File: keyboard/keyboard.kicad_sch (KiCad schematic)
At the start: 64 parts, among them J1 Conn_01x04, J2 Conn_01x04, SW1 SW_Push, SW10 SW_Push, SW11 SW_Push, SW12 SW_Push, SW13 SW_Push, SW14 SW_Push, SW15 SW_Push, SW16 SW_Push, SW17 SW_Push, SW18 SW_Push, SW19 SW_Push, SW2 SW_Push, SW20 SW_Push, SW21 SW_Push, SW3 SW_Push, SW4 SW_Push, SW5 SW_Push, SW6 SW_Push, SW7 SW_Push, SW8 SW_Push, SW9 SW_Push, U1 AP2127K-3.3, U2 USBLC6-2SC6, U3 STM32F072CBTx

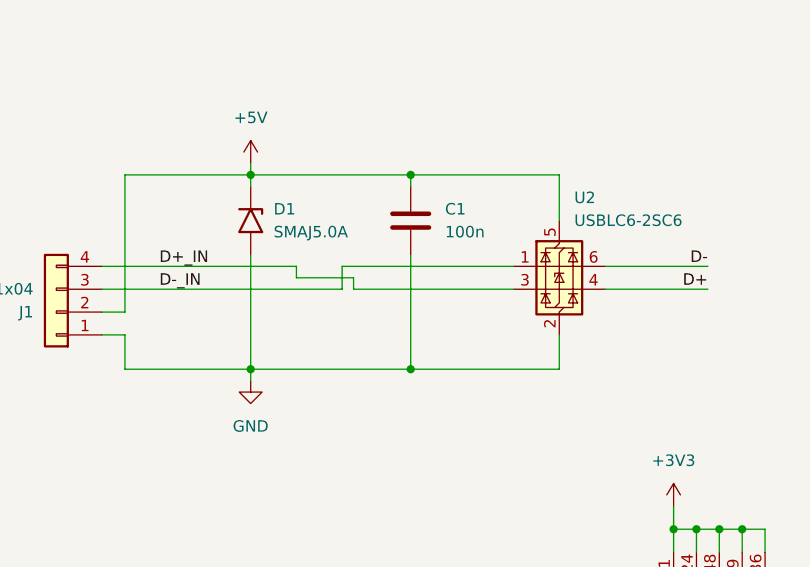
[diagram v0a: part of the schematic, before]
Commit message: Added board outlines 12mm from key switch centres.
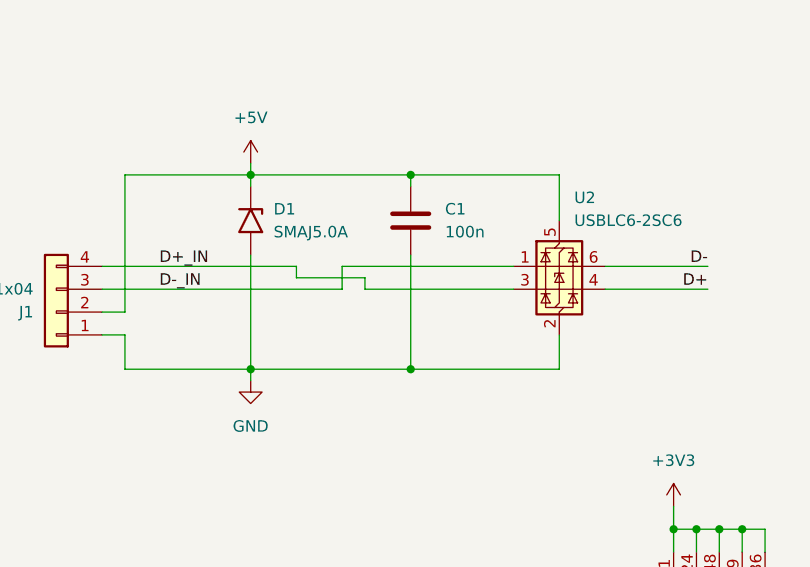
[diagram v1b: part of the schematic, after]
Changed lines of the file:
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@@
 	(wire
 		(pts
-			(xy 63.5 35.56) (xy 63.5 36.83)
+			(xy 64.77 35.56) (xy 64.77 36.83)
 		)
 		(stroke
@@
 	(wire
 		(pts
-			(xy 63.5 36.83) (xy 81.28 36.83)
+			(xy 64.77 36.83) (xy 81.28 36.83)
 		)
 		(stroke
@@
 	(wire
 		(pts
-			(xy 57.15 35.56) (xy 63.5 35.56)
-		)
-		(stroke
+			(xy 57.15 35.56) (xy 64.77 35.56)
+		)
+		(stroke

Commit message: Some routing.
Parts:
- removed SW18, SW19, SW20: SW_Push, PCM_marbastlib-mx:SW_MX_HS_KS-2P02B01-01_1.5u, symbol Switch:SW_Push
- added J3, J4: Conn_01x02, symbol Connector_Generic:Conn_01x02
- J1: footprint Connector_Wire:SolderWire-0.25sqmm_1x04_P4.5mm_D0.65mm_OD2mm_Relief -> (none)
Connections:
- net COL0: now also U3.43 (PB7); no longer U3.13 (PA3)
- net COL1: now also U3.40 (PB4); no longer U3.12 (PA2)
- net COL2: now also U3.38 (PA15); no longer U3.11 (PA1)
- net COL3: now also J4.2 (Pin_2); no longer SW15.2, SW16.2, SW17.2
- net ROW0: now also U3.46 (PB9); no longer U3.14 (PA4)
- net ROW1: now also U3.42 (PB6); no longer U3.15 (PA5)
- net ROW2: now also U3.15 (PA5); no longer U3.16 (PA6)
- net ROW3: now also U3.16 (PA6); no longer U3.17 (PA7)
- net SB_1: now reaches D18.2 (A), SW15.1, SW16.1, SW17.1
- net SB_1: now also J3.1 (Pin_1), J4.1 (Pin_1)
- new net: J3.2 (Pin_2), SW15.2, SW16.2, SW17.2
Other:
- moved on the sheet: C5, D10, D11, D12, D13, D14, D15, D16, D17, D18, D4, D5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

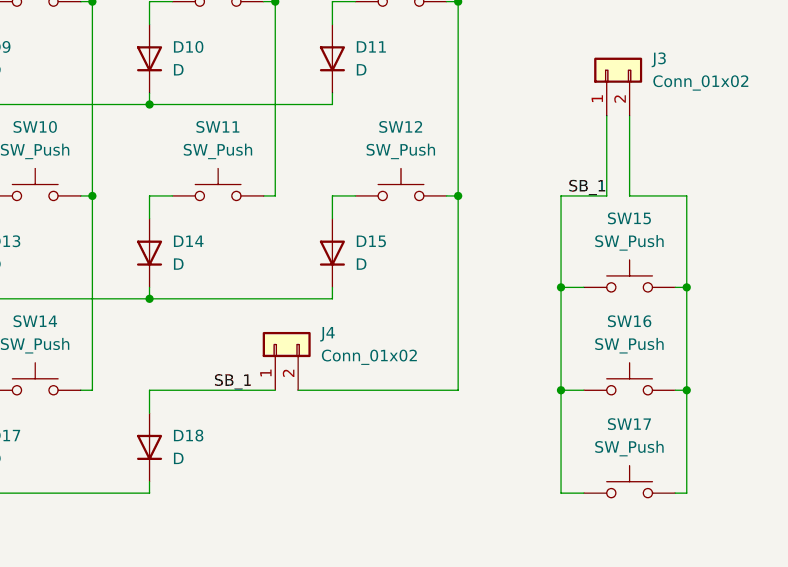
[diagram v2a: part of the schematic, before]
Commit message: Delete traces and vias before new layout.
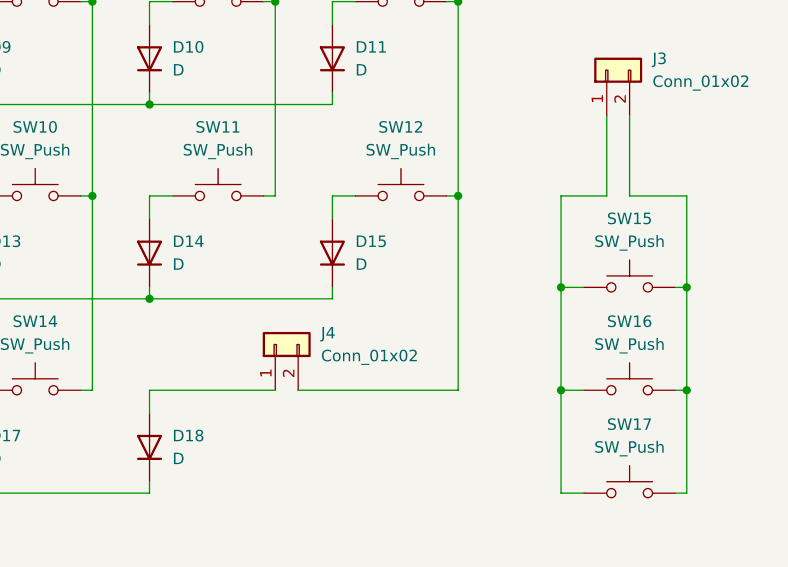
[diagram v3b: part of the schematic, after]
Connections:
- net SB_1: no longer names the net of J3.1 (Pin_1), SW15.1, SW16.1, SW17.1
- net SB_1: no longer D18.2 (A), J4.1 (Pin_1)
- new net: D18.2 (A), J4.1 (Pin_1)
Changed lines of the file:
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@@
-		)
-	)
-	(label "SB_1"
-		(at 264.16 119.38 180)
-		(effects
-			(font
-				(size 1.27 1.27)
-			)
-			(justify right bottom)
 		)
 	)
@@
 		(effects
 			(font
-				(size 1.27 1.27)
-			)
-			(justify right bottom)
-		)
-	)
-	(label "SB_1"
-		(at 224.79 140.97 180)
-		(effects
-			(font
